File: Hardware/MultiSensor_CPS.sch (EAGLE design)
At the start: 38 parts, among them U1 TCA9548APWR

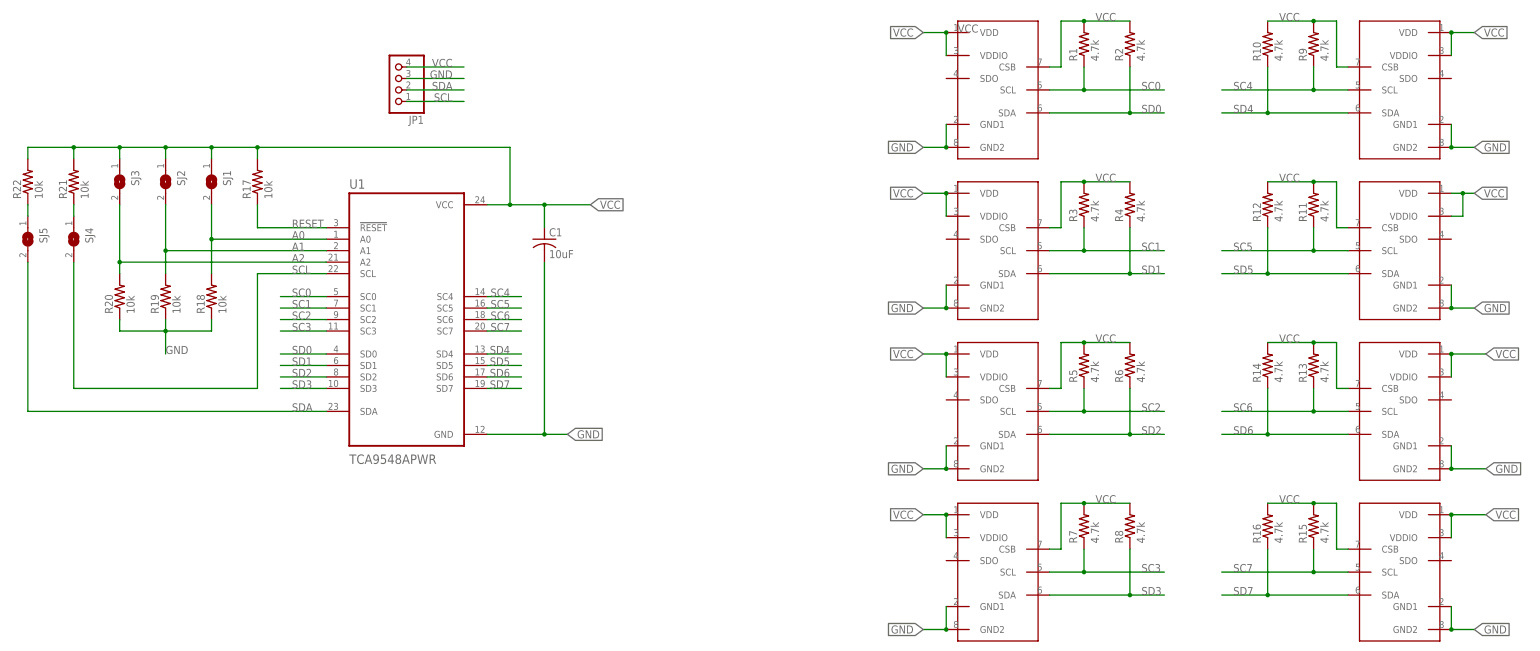
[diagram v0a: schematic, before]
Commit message: added bypass caps, routing undone
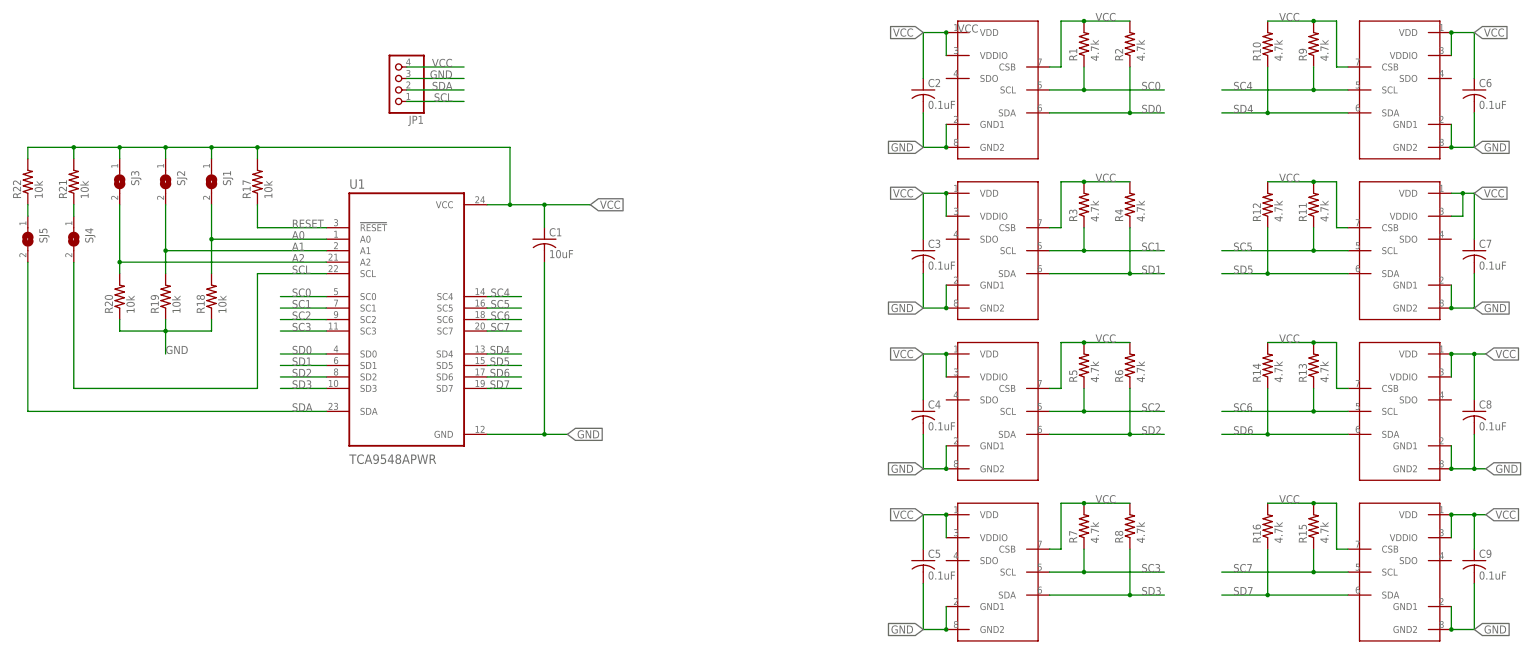
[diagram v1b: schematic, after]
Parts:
- added C2, C3, C4, C5, C6, C7, C8, C9: 0.1uF, rcl:C-USC0805
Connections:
- net GND: now also C2.2, C3.2, C4.2, C5.2, C6.2, C7.2, C8.2, C9.2
- net VCC: now also C2.1, C3.1, C4.1, C5.1, C6.1, C7.1, C8.1, C9.1
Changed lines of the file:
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@@
 <part name="R21" library="resistor" library_urn="urn:adsk.eagle:library:348" deviceset="R-US_" device="R0805" package3d_urn="urn:adsk.eagle:package:23553/2" value="10k"/>
 <part name="R22" library="resistor" library_urn="urn:adsk.eagle:library:348" deviceset="R-US_" device="R0805" package3d_urn="urn:adsk.eagle:package:23553/2" value="10k"/>
+<part name="C2" library="rcl" library_urn="urn:adsk.eagle:library:334" deviceset="C-US" device="C0805" package3d_urn="urn:adsk.eagle:package:23617/2" value="0.1uF"/>
+<part name="C3" library="rcl" library_urn="urn:adsk.eagle:library:334" deviceset="C-US" device="C0805" package3d_urn="urn:adsk.eagle:package:23617/2" value="0.1uF"/>
+<part name="C4" library="rcl" library_urn="urn:adsk.eagle:library:334" deviceset="C-US" device="C0805" package3d_urn="urn:adsk.eagle:package:23617/2" value="0.1uF"/>
+<part name="C5" library="rcl" library_urn="urn:adsk.eagle:library:334" deviceset="C-US" device="C0805" package3d_urn="urn:adsk.eagle:package:23617/2" value="0.1uF"/>
+<part name="C6" library="rcl" library_urn="urn:adsk.eagle:library:334" deviceset="C-US" device="C0805" package3d_urn="urn:adsk.eagle:package:23617/2" value="0.1uF"/>
+<part name="C7" library="rcl" library_urn="urn:adsk.eagle:library:334" deviceset="C-US" device="C0805" package3d_urn="urn:adsk.eagle:package:23617/2" value="0.1uF"/>
+<part name="C8" library="rcl" library_urn="urn:adsk.eagle:library:334" deviceset="C-US" device="C0805" package3d_urn="urn:adsk.eagle:package:23617/2" value="0.1uF"/>
+<part name="C9" library="rcl" library_urn="urn:adsk.eagle:library:334" deviceset="C-US" device="C0805" package3d_urn="urn:adsk.eagle:package:23617/2" value="0.1uF"/>
 </parts>
 <sheets>
@@
 <attribute name="NAME" x="-189.4586" y="87.63" size="1.778" layer="95" rot="R90"/>
 <attribute name="VALUE" x="-184.658" y="87.63" size="1.778" layer="96" rot="R90"/>
+</instance>
+<instance part="C2" gate="G$1" x="10.16" y="111.76" smashed="yes">
+<attribute name="NAME" x="11.176" y="112.395" size="1.778" layer="95"/>
+<attribute name="VALUE" x="11.176" y="107.569" size="1.778" layer="96"/>
+</instance>
+<instance part="C3" gate="G$1" x="10.16" y="76.2" smashed="yes">
+<attribute name="NAME" x="11.176" y="76.835" size="1.778" layer="95"/>
+<attribute name="VALUE" x="11.176" y="72.009" size="1.778" layer="96"/>
+</instance>
+<instance part="C4" gate="G$1" x="10.16" y="40.64" smashed="yes">
+<attribute name="NAME" x="11.176" y="41.275" size="1.778" layer="95"/>
+<attribute name="VALUE" x="11.176" y="36.449" size="1.778" layer="96"/>
+</instance>
+<instance part="C5" gate="G$1" x="10.16" y="7.62" smashed="yes">
+<attribute name="NAME" x="11.176" y="8.255" size="1.778" layer="95"/>
+<attribute name="VALUE" x="11.176" y="3.429" size="1.778" layer="96"/>
+</instance>
+<instance part="C6" gate="G$1" x="132.08" y="111.76" smashed="yes">
+<attribute name="NAME" x="133.096" y="112.395" size="1.778" layer="95"/>
+<attribute name="VALUE" x="133.096" y="107.569" size="1.778" layer="96"/>
+</instance>
+<instance part="C7" gate="G$1" x="132.08" y="76.2" smashed="yes">
+<attribute name="NAME" x="133.096" y="76.835" size="1.778" layer="95"/>
+<attribute name="VALUE" x="133.096" y="72.009" size="1.778" layer="96"/>
+</instance>
+<instance part="C8" gate="G$1" x="132.08" y="40.64" smashed="yes">
+<attribute name="NAME" x="133.096" y="41.275" size="1.778" layer="95"/>
+<attribute name="VALUE" x="133.096" y="36.449" size="1.778" layer="96"/>
+</instance>
+<instance part="C9" gate="G$1" x="132.08" y="7.62" smashed="yes">
+<attribute name="NAME" x="133.096" y="8.255" size="1.778" layer="95"/>
+<attribute name="VALUE" x="133.096" y="3.429" size="1.778" layer="96"/>
 </instance>
 </instances>
@@
 <wire x1="15.24" y1="119.38" x2="15.24" y2="124.46" width="0.1524" layer="91"/>
 <junction x="15.24" y="124.46"/>
+<pinref part="C2" gate="G$1" pin="1"/>
+<wire x1="10.16" y1="114.3" x2="10.16" y2="124.46" width="0.1524" layer="91"/>
 </segment>
 <segment>
@@
 <wire x1="15.24" y1="83.82" x2="15.24" y2="88.9" width="0.1524" layer="91"/>
 <junction x="15.24" y="88.9"/>
+<pinref part="C3" gate="G$1" pin="1"/>
+<wire x1="10.16" y1="78.74" x2="10.16" y2="88.9" width="0.1524" layer="91"/>
 </segment>
 <segment>
@@
 <wire x1="15.24" y1="48.26" x2="15.24" y2="53.34" width="0.1524" layer="91"/>
 <junction x="15.24" y="53.34"/>
+<pinref part="C4" gate="G$1" pin="1"/>
+<wire x1="10.16" y1="43.18" x2="10.16" y2="53.34" width="0.1524" layer="91"/>
 </segment>
 <segment>
@@
 <wire x1="15.24" y1="12.7" x2="15.24" y2="17.78" width="0.1524" layer="91"/>
 <junction x="15.24" y="17.78"/>
+<pinref part="C5" gate="G$1" pin="1"/>
+<wire x1="10.16" y1="10.16" x2="10.16" y2="17.78" width="0.1524" layer="91"/>
 </segment>
 <segment>
@@
 <wire x1="129.54" y1="83.82" x2="129.54" y2="88.9" width="0.1524" layer="91"/>
 <junction x="129.54" y="88.9"/>
+<pinref part="C7" gate="G$1" pin="1"/>
+<wire x1="132.08" y1="78.74" x2="132.08" y2="88.9" width="0.1524" layer="91"/>
 </segment>
 <segment>
@@
 <wire x1="127" y1="119.38" x2="127" y2="124.46" width="0.1524" layer="91"/>
 <junction x="127" y="124.46"/>
+<pinref part="C6" gate="G$1" pin="1"/>
+<wire x1="132.08" y1="114.3" x2="132.08" y2="124.46" width="0.1524" layer="91"/>
 </segment>
 <segment>
@@
 <label x="134.62" y="53.34" size="1.778" layer="95" xref="yes"/>
 <pinref part="B3" gate="G$1" pin="VDDIO"/>
-<wire x1="127" y1="53.34" x2="134.62" y2="53.34" width="0.1524" layer="91"/>
+<wire x1="127" y1="53.34" x2="132.08" y2="53.34" width="0.1524" layer="91"/>
+<wire x1="132.08" y1="53.34" x2="134.62" y2="53.34" width="0.1524" layer="91"/>
 <wire x1="127" y1="48.26" x2="127" y2="53.34" width="0.1524" layer="91"/>
 <junction x="127" y="53.34"/>
+<pinref part="C8" gate="G$1" pin="1"/>
+<wire x1="132.08" y1="43.18" x2="132.08" y2="53.34" width="0.1524" layer="91"/>
+<junction x="132.08" y="53.34"/>
 </segment>
 <segment>
@@
 <label x="134.62" y="17.78" size="1.778" layer="95" xref="yes"/>
 <pinref part="B8" gate="G$1" pin="VDDIO"/>
-<wire x1="127" y1="17.78" x2="134.62" y2="17.78" width="0.1524" layer="91"/>
+<wire x1="127" y1="17.78" x2="132.08" y2="17.78" width="0.1524" layer="91"/>
+<wire x1="132.08" y1="17.78" x2="134.62" y2="17.78" width="0.1524" layer="91"/>
 <wire x1="127" y1="17.78" x2="127" y2="12.7" width="0.1524" layer="91"/>
 <junction x="127" y="17.78"/>
+<pinref part="C9" gate="G$1" pin="1"/>
+<wire x1="132.08" y1="10.16" x2="132.08" y2="17.78" width="0.1524" layer="91"/>
+<junction x="132.08" y="17.78"/>
 </segment>
 <segment>
@@
 <wire x1="127" y1="104.14" x2="127" y2="99.06" width="0.1524" layer="91"/>
 <junction x="127" y="99.06"/>
+<pinref part="C6" gate="G$1" pin="2"/>
+<wire x1="132.08" y1="106.68" x2="132.08" y2="99.06" width="0.1524" layer="91"/>
 </segment>
 <segment>
@@
 <wire x1="15.24" y1="104.14" x2="15.24" y2="99.06" width="0.1524" layer="91"/>
 <junction x="15.24" y="99.06"/>
+<pinref part="C2" gate="G$1" pin="2"/>
+<wire x1="10.16" y1="106.68" x2="10.16" y2="99.06" width="0.1524" layer="91"/>
 </segment>
 <segment>
@@
 <wire x1="15.24" y1="68.58" x2="15.24" y2="63.5" width="0.1524" layer="91"/>
 <junction x="15.24" y="63.5"/>
+<pinref part="C3" gate="G$1" pin="2"/>
+<wire x1="10.16" y1="71.12" x2="10.16" y2="63.5" width="0.1524" layer="91"/>
 </segment>
 <segment>
@@
 <wire x1="15.24" y1="33.02" x2="15.24" y2="27.94" width="0.1524" layer="91"/>
 <junction x="15.24" y="27.94"/>
+<pinref part="C4" gate="G$1" pin="2"/>
+<wire x1="10.16" y1="35.56" x2="10.16" y2="27.94" width="0.1524" layer="91"/>
 </segment>
 <segment>
@@
 <wire x1="15.24" y1="-2.54" x2="15.24" y2="-7.62" width="0.1524" layer="91"/>
 <junction x="15.24" y="-7.62"/>
+<pinref part="C5" gate="G$1" pin="2"/>
+<wire x1="10.16" y1="2.54" x2="10.16" y2="-7.62" width="0.1524" layer="91"/>
 </segment>
 <segment>
@@
 <wire x1="127" y1="-2.54" x2="127" y2="-7.62" width="0.1524" layer="91"/>
 <junction x="127" y="-7.62"/>
+<pinref part="C9" gate="G$1" pin="2"/>
+<wire x1="132.08" y1="2.54" x2="132.08" y2="-7.62" width="0.1524" layer="91"/>
 </segment>
 <segment>
@@
 <pinref part="B3" gate="G$1" pin="GND2"/>
 <label x="134.62" y="27.94" size="1.778" layer="95" xref="yes"/>
-<wire x1="127" y1="27.94" x2="134.62" y2="27.94" width="0.1524" layer="91"/>
+<wire x1="127" y1="27.94" x2="132.08" y2="27.94" width="0.1524" layer="91"/>
+<wire x1="132.08" y1="27.94" x2="134.62" y2="27.94" width="0.1524" layer="91"/>
 <wire x1="127" y1="33.02" x2="127" y2="27.94" width="0.1524" layer="91"/>
 <junction x="127" y="27.94"/>
+<pinref part="C8" gate="G$1" pin="2"/>
+<wire x1="132.08" y1="35.56" x2="132.08" y2="27.94" width="0.1524" layer="91"/>
+<junction x="132.08" y="27.94"/>
 </segment>
 <segment>
@@
 <wire x1="127" y1="68.58" x2="127" y2="63.5" width="0.1524" layer="91"/>
 <junction x="127" y="63.5"/>
-</segment>
-<segment>
+<pinref part="C7" gate="G$1" pin="2"/>
+<wire x1="132.08" y1="71.12" x2="132.08" y2="63.5" width="0.1524" layer="91"/>
+</segment>
+<segment>
